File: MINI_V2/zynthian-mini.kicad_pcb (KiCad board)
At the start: 2 copper layers, 163 x 120 mm, 92 parts, among them J1 NEUTRIK, J2 NEUTRIK, J3 Conn_02x04_Odd_Even, J4 Conn_01x05, J6 TRRS-PJ-320A, J7 TRRS-PJ-320A, SW1 SW_Push, SW10 SW_Push, SW11 SW_Push, SW12 SW_Push, SW13 SW_Push, SW14 SW_Push, SW15 SW_Push, SW16 SW_Push, SW17 SW_Push, SW18 SW_Push, SW19 SW_Push, SW2 SW_Push, SW20 SW_Push, SW3 SW_Push, SW4 SW_Push, SW5 SW_Push, SW6 SW_Push, SW7 SW_Push, SW8 SW_Push, SW9 SW_Push, U1 74HCT14, U2 H11L1M

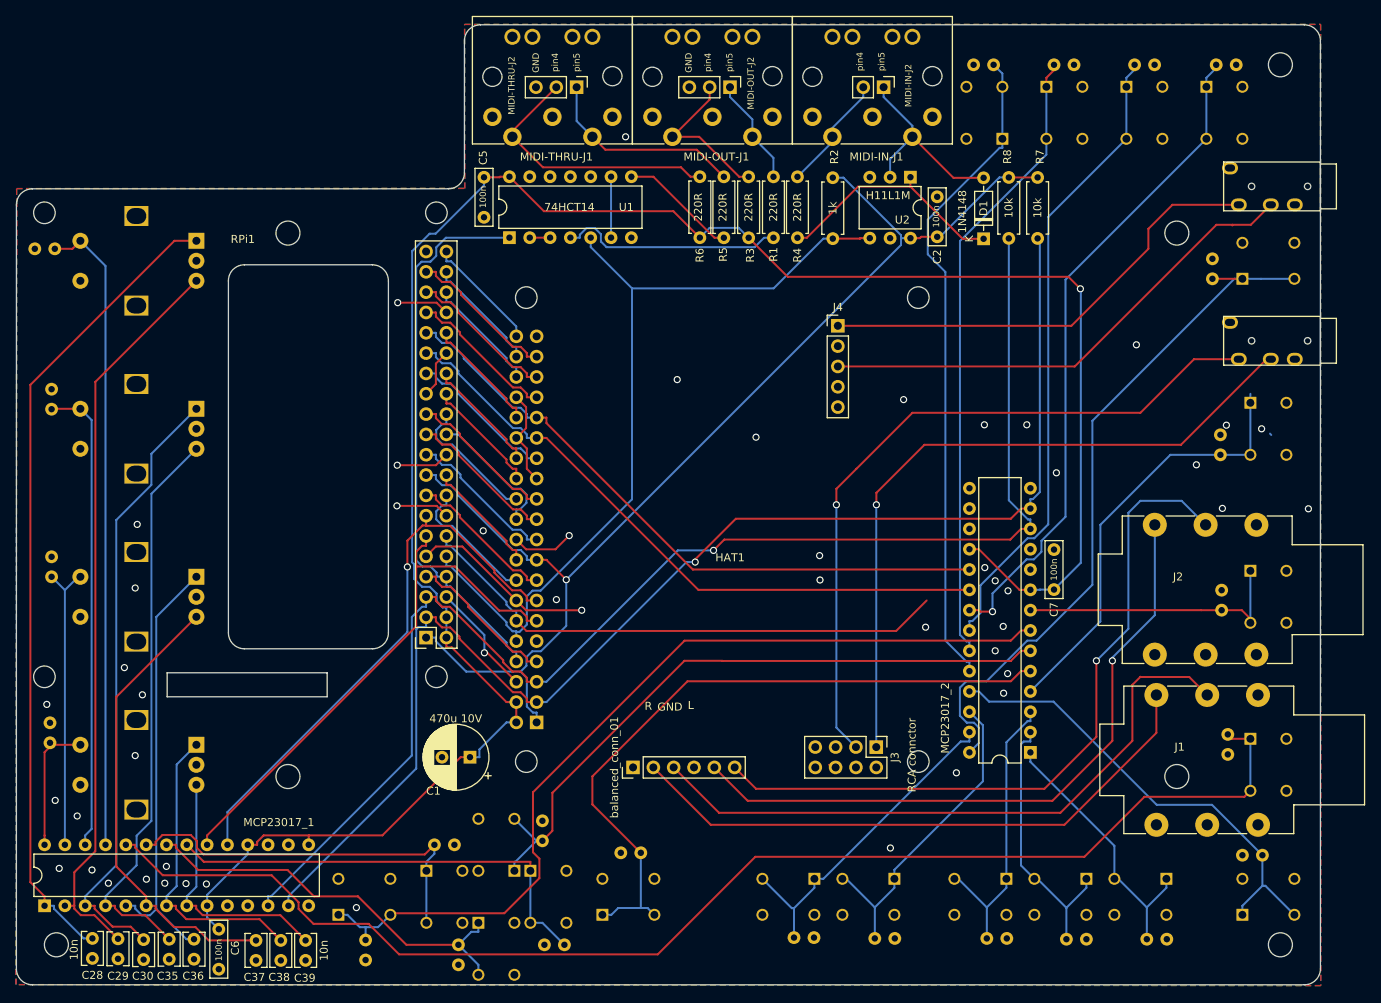
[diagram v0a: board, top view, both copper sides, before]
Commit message: moved 6.3 jacks to free screen hole
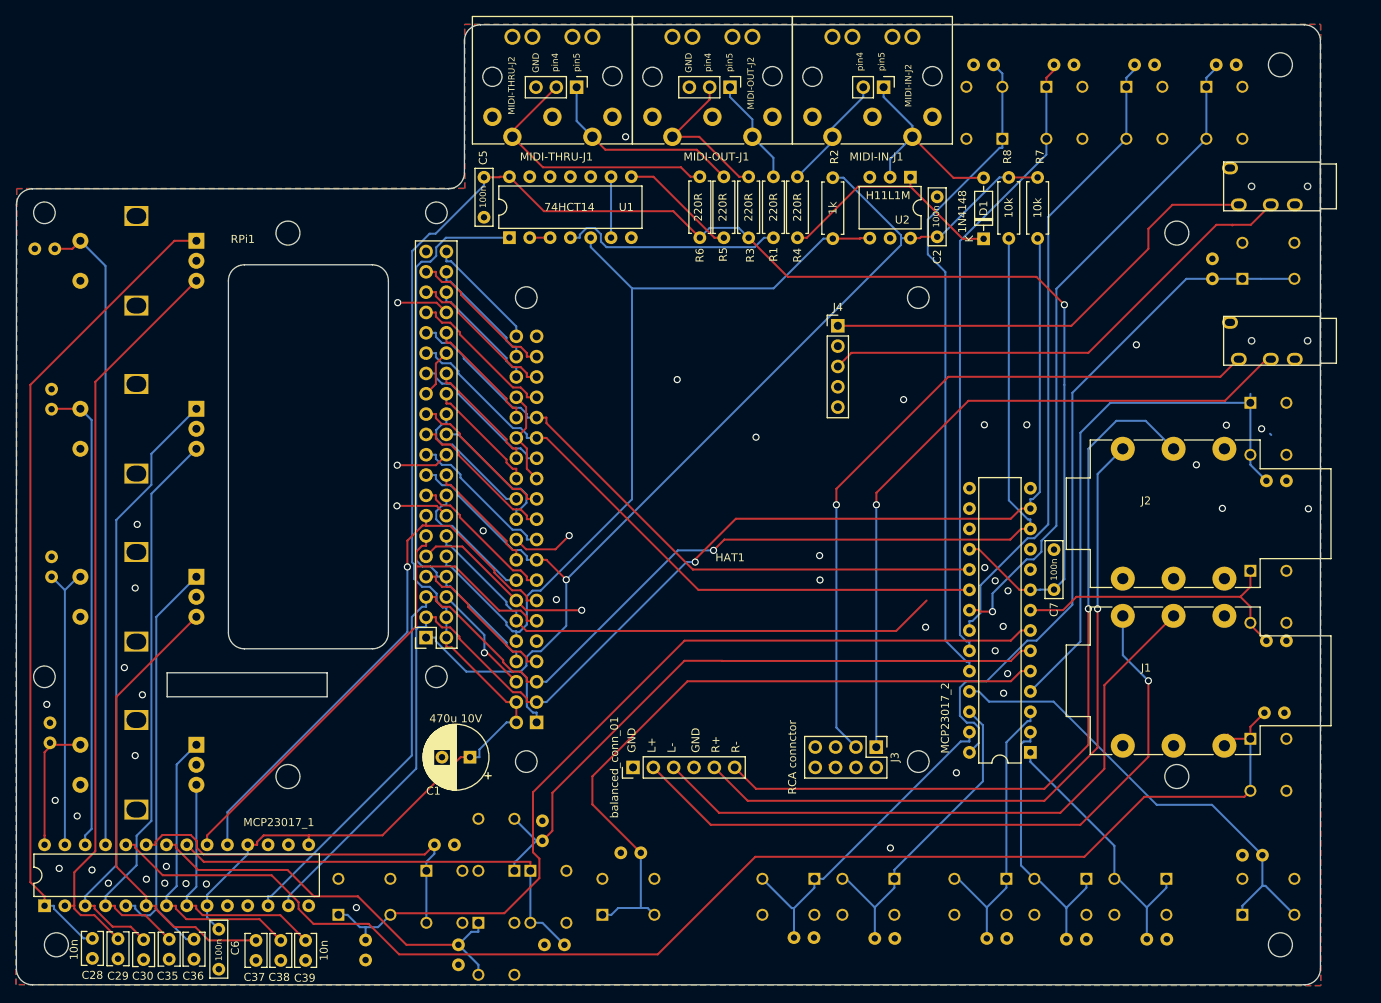
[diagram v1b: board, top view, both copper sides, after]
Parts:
- moved J1 10.7 mm to (171.7, 109.3)
- moved J2 10.3 mm to (171.7, 88.4)
- moved C23 6.78 mm to (189.7, 112.4), turned to 0 degrees
- moved C17 6.60 mm to (189.7, 92.4), turned to 0 degrees
- moved C27 5.31 mm to (189.4, 121.4), turned to 0 degrees
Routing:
- net SWITCH-12: track 54.8 -> 69.8 mm
- net AUDIO_L_PLUS: track 75.3 -> 87.3 mm, vias 0 -> 1
- net AUDIO_R_MINUS: track 90.8 -> 98.2 mm
- net AUDIO_R_PLUS: track 83.8 -> 91.0 mm
- net +5V: track 267.9 -> 263.8 mm
- net SWITCH-20: track 165.0 -> 168.9 mm
- net SWITCH-16: track 35.2 -> 37.6 mm
- net GND: vias 50 -> 49
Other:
- board text added: "L+"
- board text added: "L-"
- board text added: "R+"
- board text added: "R-"
- board text removed: "L"
- board text removed: "R"

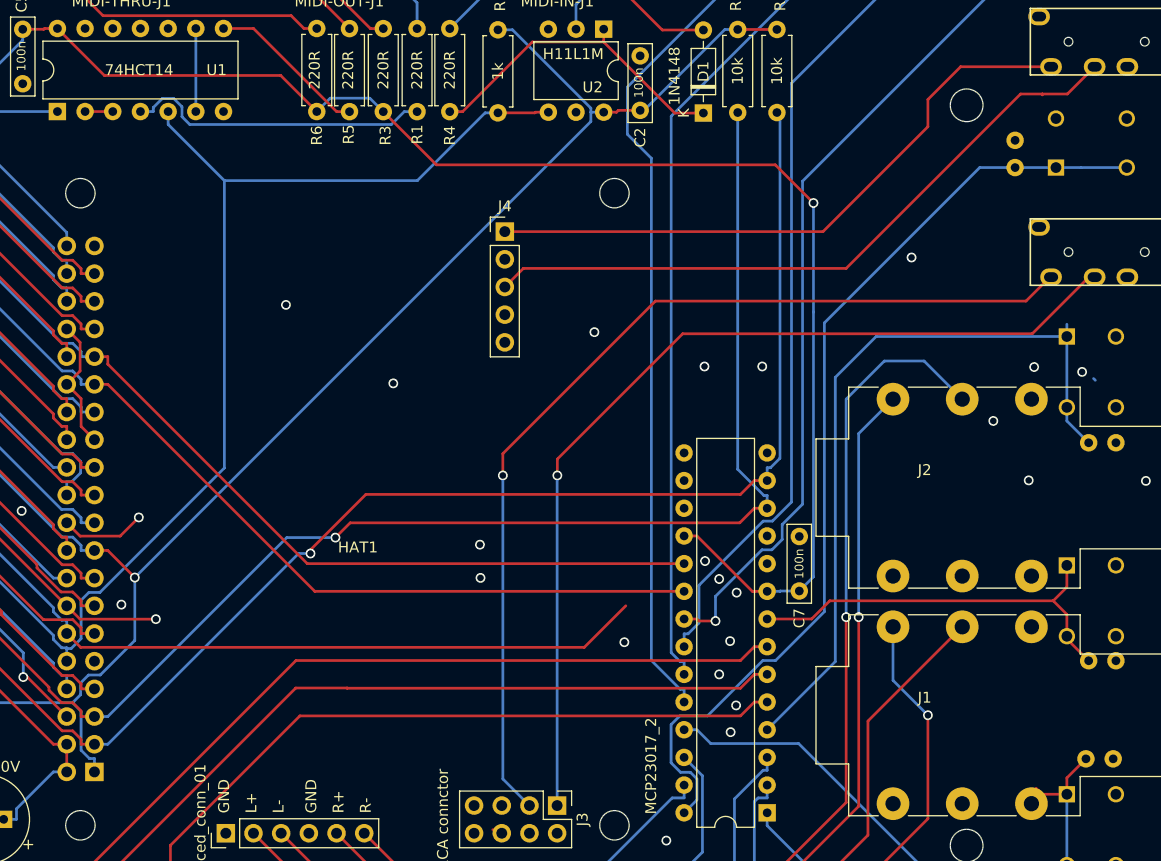
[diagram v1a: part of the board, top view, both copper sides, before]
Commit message: fixed "design rules checker"
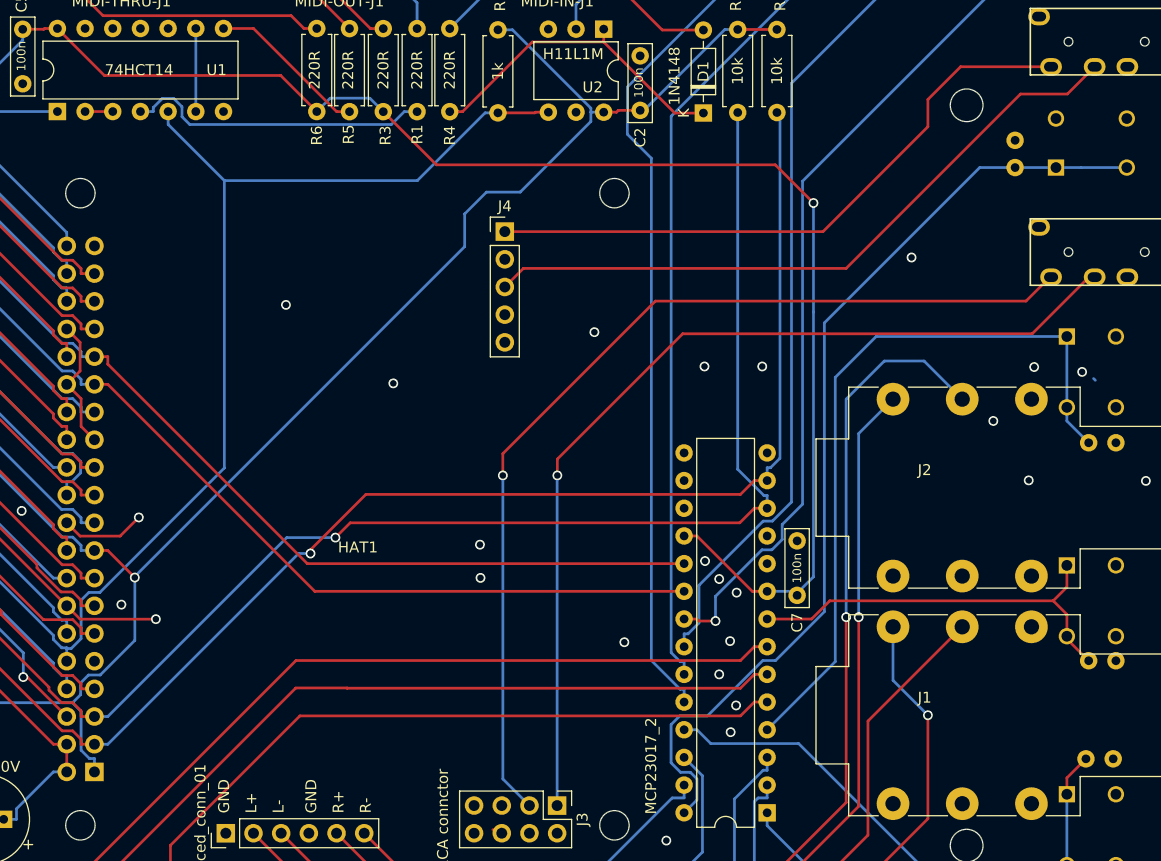
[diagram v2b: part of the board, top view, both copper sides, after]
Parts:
- moved logo1 5.51 mm to (119.9, 76.4)
- moved REF** 2.05 mm to (119.4, 71.9)
- moved C7 0.45 mm to (162.9, 106.4)
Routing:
- net I2S_BCLK: track 68.2 -> 14.8 mm
- net SWITCH-20: track 168.9 -> 165.9 mm
- net +3.3V: track 151.6 -> 153.4 mm
- net SWITCH-12: track 69.8 -> 68.7 mm
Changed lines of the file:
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@@
 	(footprint "project-footprints:C_Rect_L7.0mm_W2.0mm_P5.00mm"
 		(layer "F.Cu")
-		(at 163.1193 105.9736 90)
+		(at 162.9193 106.3736 90)
 		(descr "C, Rect series, Radial, pin pitch=5.00mm, , length*width=7*2mm^2, Capacitor")
 		(tags "C Rect series Radial pin pitch 5.00mm  length 7mm width 2mm Capacitor")
@@
 	(footprint "Symbol:OSHW-Logo2_7.3x6mm_SilkScreen"
 		(layer "B.Cu")
-		(at 120.153286 73.782489 180)
+		(at 119.4193 71.8736 180)
 		(descr "Open Source Hardware Symbol")
 		(tags "Logo Symbol OSHW")
@@
 		)
 		(property "Value" "100n"
-			(at 1.4 2.425 0)
+			(at 1.25 -2.5 0)
 			(layer "B.SilkS")
 			(effects
@@
 	(footprint "project-footprints:Zynthian Logo Mask"
 		(layer "B.Cu")
-		(at 121.0193 81.7736 180)
+		(at 119.9193 76.3736 180)
 		(property "Reference" "logo1"
 			(at 5.525 3.3 180)
@@
 	)
 	(gr_text "rev2"
-		(at 115.4193 85.8736 0)
+		(at 114.9193 80.3736 0)
 		(layer "B.SilkS")
 		(effects
@@
 	)
 	(segment
-		(start 160.1693 106.0036)
-		(end 161.346 106.0036)
-		(width 0.25)
-		(layer "B.Cu")
-		(net 2)
-	)
-	(segment
 		(start 163.1193 105.9736)
 		(end 164.4193 104.6736)
@@
 	)
 	(segment
+		(start 160.1693 106.0036)
+		(end 162.5493 106.0036)
+		(width 0.25)
+		(layer "B.Cu")
+		(net 2)
+	)
+	(segment
 		(start 82.8827 63.6744)
 		(end 85.0737 61.4834)
@@
 	)
 	(segment
-		(start 163.1193 105.9736)
-		(end 161.376 105.9736)
+		(start 91.8693 55.4407)
+		(end 91.8693 54.4336)
 		(width 0.25)
 		(layer "B.Cu")
@@
 	)
 	(segment
-		(start 91.8693 55.4407)
-		(end 91.8693 54.4336)
+		(start 162.5493 106.0036)
+		(end 162.9193 106.3736)
 		(width 0.25)
 		(layer "B.Cu")
@@
 	)
 	(segment
-		(start 161.376 105.9736)
-		(end 161.346 106.0036)
-		(width 0.25)
-		(layer "B.Cu")
-		(net 2)
-	)
-	(segment
 		(start 84.1351 105.6236)
 		(end 83.1252 104.6137)
@@
 	)
 	(segment
+		(start 132.4193 71.3736)
+		(end 132.4193 74.3736)
+		(width 0.25)
+		(layer "B.Cu")
+		(net 12)
+	)
+	(segment
 		(start 97.9867 121.3469)
 		(end 98.4468 121.3469)
@@
 	)
 	(segment
+		(start 102.1501 104.6428)
+		(end 102.1501 104.739)
+		(width 0.25)
+		(layer "B.Cu")
+		(net 12)
+	)
+	(segment
 		(start 97.1768 115.4902)
 		(end 96.4434 116.2236)
@@
 	)
 	(segment
+		(start 132.4193 74.3736)
+		(end 102.1501 104.6428)
+		(width 0.25)
+		(layer "B.Cu")
+		(net 12)
+	)
+	(segment
 		(start 88.6448 93.8725)
 		(end 87.6959 92.9236)
@@
 	)
 	(segment
+		(start 134.4193 69.3736)
+		(end 132.4193 71.3736)
+		(width 0.25)
+		(layer "B.Cu")
+		(net 12)
+	)
+	(segment
 		(start 97.902 113.6836)
 		(end 97.1768 114.4088)
@@
 	)
 	(segment
-		(start 102.1501 104.739)
-		(end 143.9976 62.8915)
-		(width 0.25)
-		(layer "B.Cu")
-		(net 12)
-	)
-	(segment
 		(start 86.6177 92.9236)
 		(end 85.856 92.1619)
@@
 	)
 	(segment
+		(start 137.5155 69.3736)
+		(end 134.4193 69.3736)
+		(width 0.25)
+		(layer "B.Cu")
+		(net 12)
+	)
+	(segment
 		(start 98.9738 113.6836)
 		(end 97.902 113.6836)
@@
 	)
 	(segment
+		(start 143.9976 62.8915)
+		(end 137.5155 69.3736)
+		(width 0.25)
+		(layer "B.Cu")
+		(net 12)
+	)
+	(segment
 		(start 97.2201 102.2536)
 		(end 97.2201 101.7935)
@@
 	)
 	(segment
-		(start 143.3913 111.1436)
-		(end 147.2024 107.3325)
-		(width 0.25)
-		(layer "F.Cu")
-		(net 16)
-	)
-	(segment
-		(start 95.9068 109.8736)
-		(end 97.1768 111.1436)
-		(width 0.25)
-		(layer "F.Cu")
-		(net 16)
-	)
-	(segment
-		(start 97.1768 111.1436)
-		(end 143.3913 111.1436)
-		(width 0.25)
-		(layer "F.Cu")
-		(net 16)
-	)
-	(segment
 		(start 95.9068 108.6469)
 		(end 95.4467 108.6469)
@@
 	)
 	(segment
-		(start 187.6693 82.6236)
-		(end 187.6693 81.4979)
-		(width 0.25)
-		(layer "B.Cu")
-		(net 51)
-	)
-	(segment
 		(start 187.6693 89.1236)
 		(end 187.6693 90.3736)
@@
 	)
 	(segment
-		(start 187.6693 124.6236)
-		(end 185.3943 124.6236)
-		(width 0.25)
-		(layer "F.Cu")
-		(net 59)
-	)
-	(segment
 		(start 113.5864 151.5707)
 		(end 125.7835 139.3736)
@@
 	)
 	(segment
-		(start 185.3943 124.6236)
-		(end 184.8443 124.0736)
-		(width 0.25)
-		(layer "F.Cu")
-		(net 59)
-	)
-	(segment
 		(start 68.6893 145.0482)
 		(end 68.6893 145.8905)
@@
 	)
 	(segment
-		(start 183.4193 60.3736)
-		(end 167.4193 76.3736)
+		(start 187.7193 60.3736)
+		(end 183.4193 60.3736)
 		(width 0.25)
 		(layer "F.Cu")
@@
 	)
 	(segment
-		(start 185.4193 60.3736)
+		(start 190.2193 57.8736)
 		(end 187.7193 60.3736)
 		(width 0.25)
@@
 	)
 	(segment
-		(start 137.8064 76.3736)
-		(end 136.1 78.08)
-		(width 0.25)
-		(layer "F.Cu")
-		(net 108)
-	)
-	(segment
-		(start 185.4193 60.460484)
-		(end 185.4193 60.3736)
-		(width 0.25)
-		(layer "F.Cu")
-		(net 108)
-	)
-	(segment
-		(start 185.4193 60.3736)
-		(end 183.4193 60.3736)
+		(start 183.4193 60.3736)
+		(end 167.4193 76.3736)
 		(width 0.25)
 		(layer "F.Cu")
@@
 	)
 	(segment
-		(start 187.7193 60.3736)
-		(end 190.2193 57.8736)
+		(start 137.8064 76.3736)
+		(end 136.1 78.08)
 		(width 0.25)
 		(layer "F.Cu")

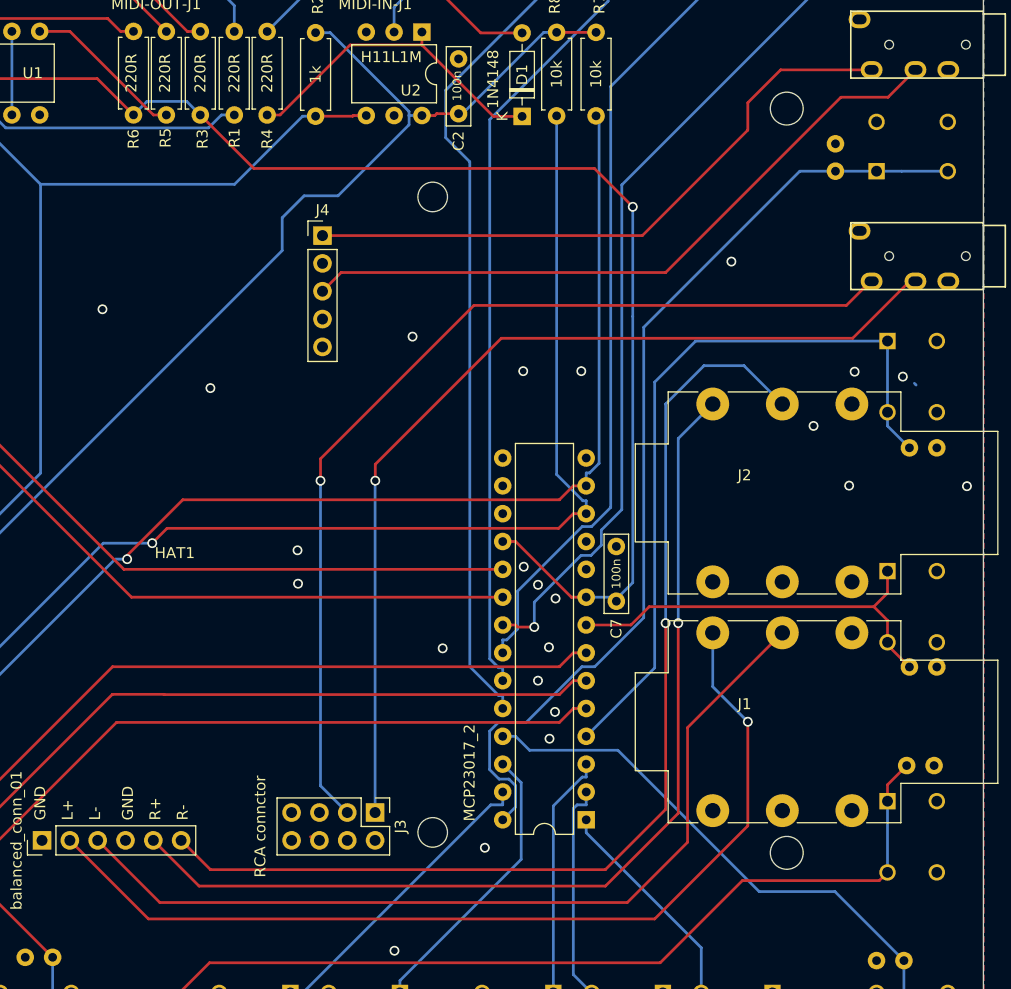
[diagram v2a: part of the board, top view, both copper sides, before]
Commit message: thicker audio signals
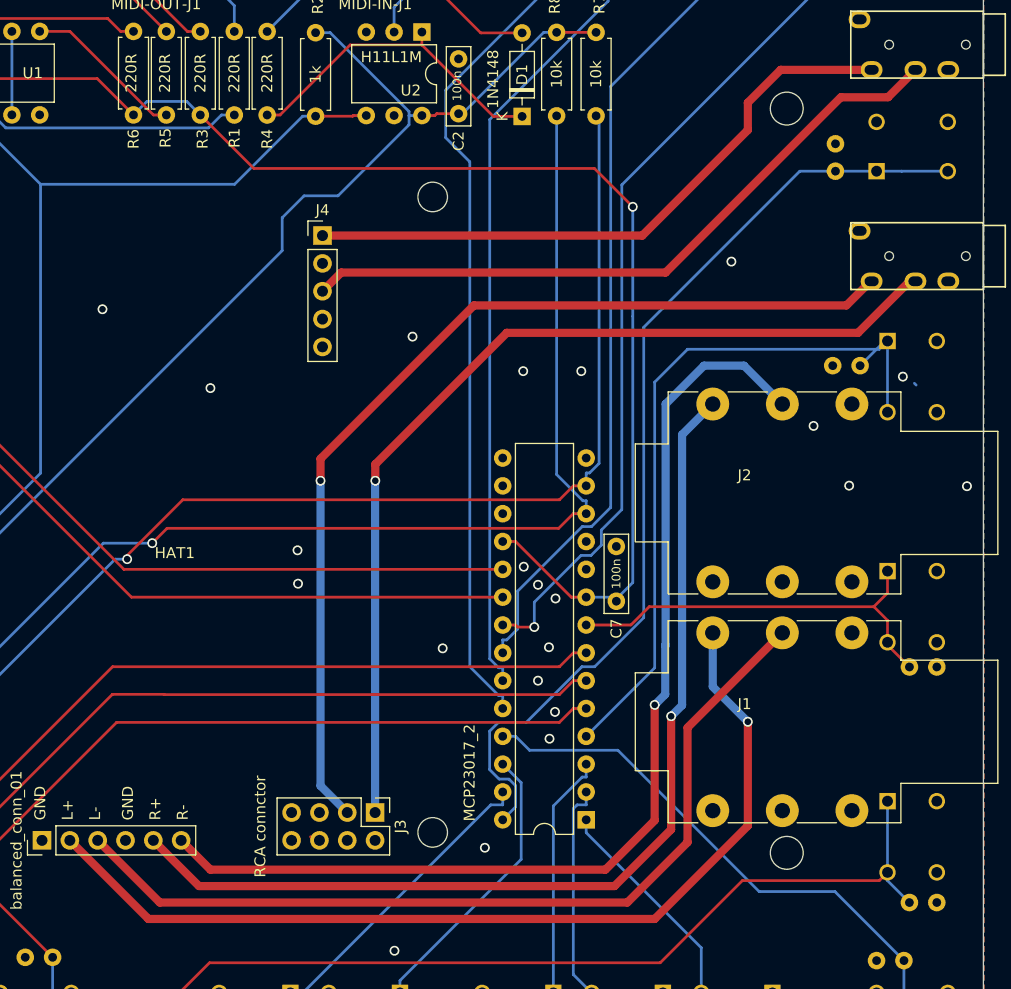
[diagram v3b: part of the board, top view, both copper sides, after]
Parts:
- moved C27 12.5 mm to (189.7, 133.9)
- moved C17 8.75 mm to (185.2, 84.9), turned to 180 degrees
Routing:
- net GND: vias 49 -> 48
